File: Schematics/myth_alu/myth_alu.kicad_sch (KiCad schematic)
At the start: 5 parts, among them U1 74AHC273, U2 74AHC273, U3 SST39SF040, U4 74HC04, U5 SST39SF040

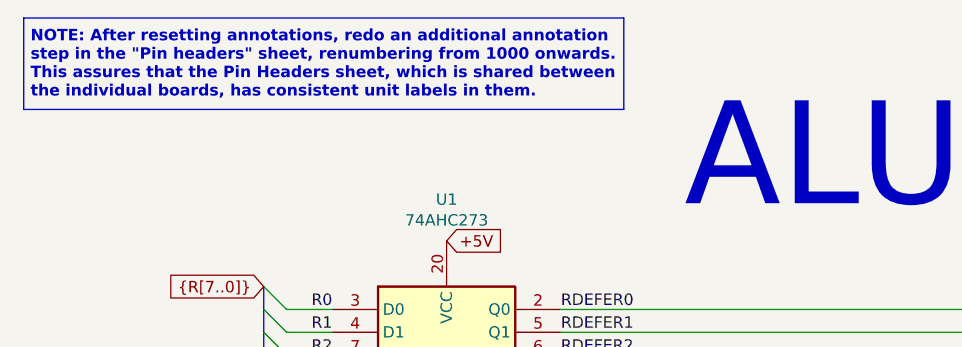
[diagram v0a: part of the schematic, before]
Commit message: Reduce number of shared headers
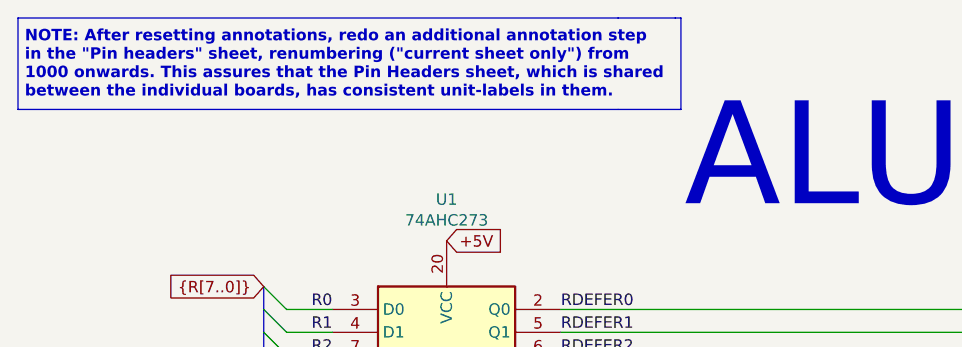
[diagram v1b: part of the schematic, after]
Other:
- note added: "NOTE: After resetting annotations, redo an additional annotation step in the "Pin headers" sheet, renumbering ("current sheet only") from 1000 onwards. This assures that the Pin Headers sheet, which is shared between the individual boards, has consistent unit-labels in them."
- note removed: "NOTE: After resetting annotations, redo an additional annotation step in the "Pin headers" sheet, renumbering from 1000 onwards. This assures that the Pin Headers sheet, which is shared between the individual boards, has consistent unit labels in them."

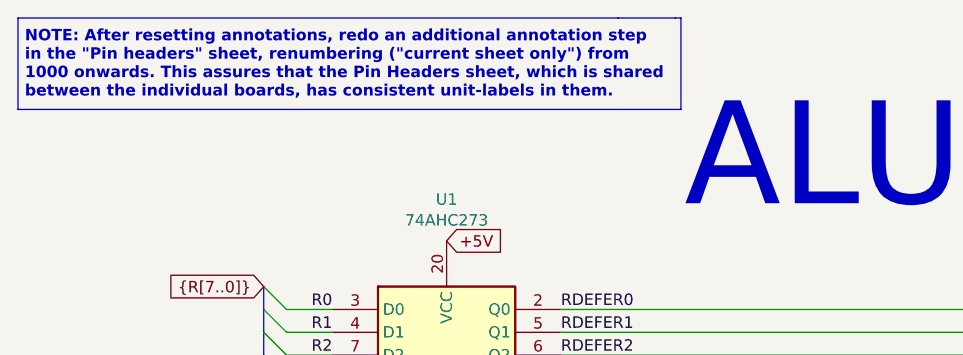
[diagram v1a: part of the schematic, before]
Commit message: Improve schematics for readability
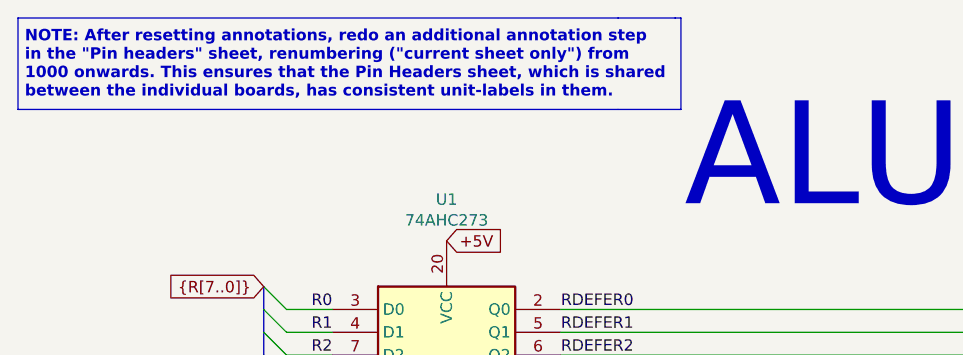
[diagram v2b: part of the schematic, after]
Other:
- note added: "NOTE: After resetting annotations, redo an additional annotation step in the "Pin headers" sheet, renumbering ("current sheet only") from 1000 onwards. This ensures that the Pin Headers sheet, which is shared between the individual boards, has consistent unit-labels in them."
- note removed: "NOTE: After resetting annotations, redo an additional annotation step in the "Pin headers" sheet, renumbering ("current sheet only") from 1000 onwards. This assures that the Pin Headers sheet, which is shared between the individual boards, has consistent unit-labels in them."
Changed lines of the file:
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@@
 		)
 	)
-	(text "NOTE: After resetting annotations, redo an additional annotation step\nin the \"Pin headers\" sheet, renumbering (\"current sheet only\") from\n1000 onwards. This assures that the Pin Headers sheet, which is shared\nbetween the individual boards, has consistent unit-labels in them."
+	(text "NOTE: After resetting annotations, redo an additional annotation step\nin the \"Pin headers\" sheet, renumbering (\"current sheet only\") from\n1000 onwards. This ensures that the Pin Headers sheet, which is shared\nbetween the individual boards, has consistent unit-labels in them."
 		(exclude_from_sim no)
 		(at 14.097 22.352 0)

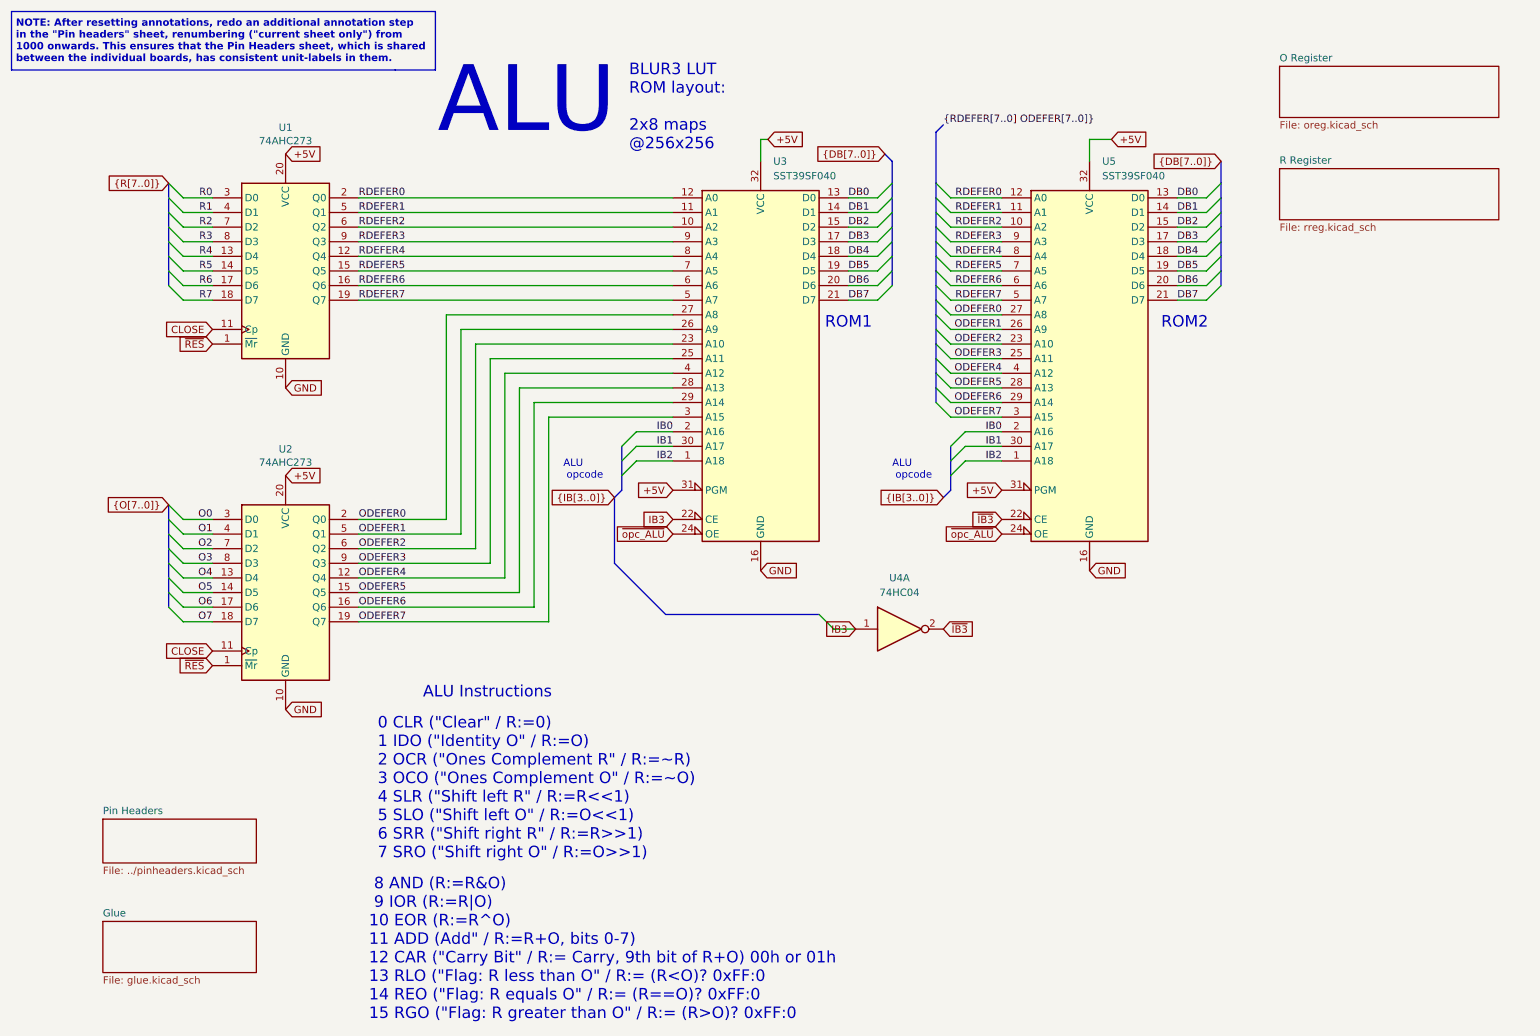
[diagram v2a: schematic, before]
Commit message: Change d to g
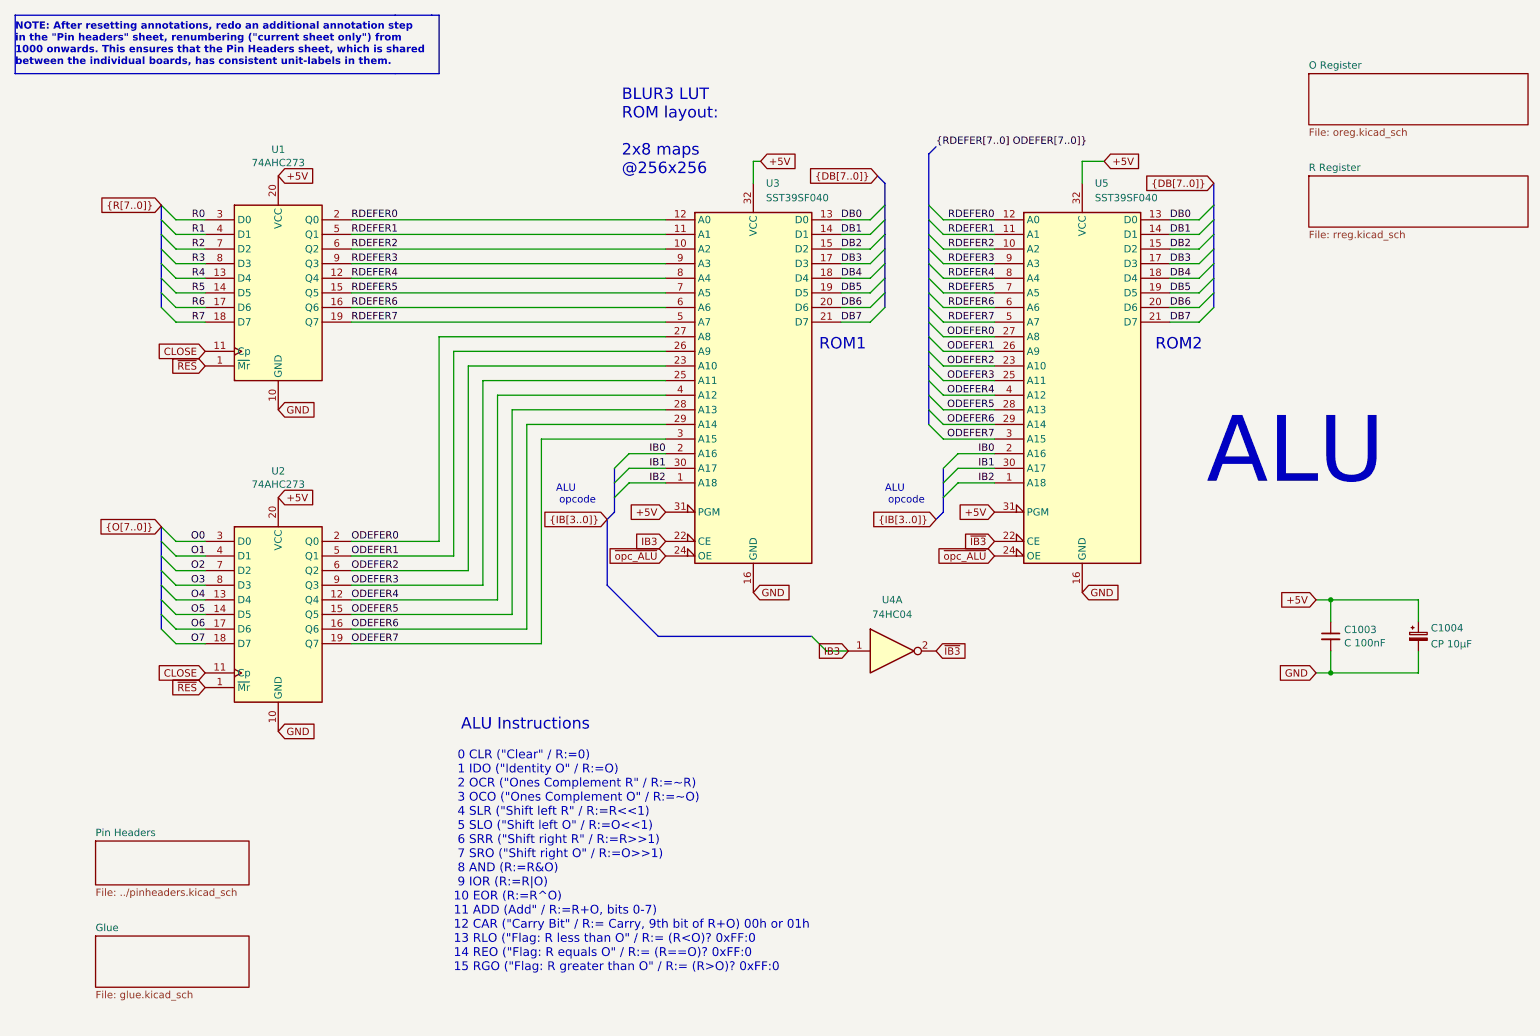
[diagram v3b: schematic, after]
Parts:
- added C1003: C 100nF, Capacitor_THT:C_Disc_D5.0mm_W2.5mm_P2.50mm, symbol Device:C_Small
- added C1004: CP 10μF, Capacitor_THT:CP_Radial_D6.3mm_P2.50mm, symbol Device:C_Polarized_Small
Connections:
- net +5V: now also C1003.1, C1004.1
- net GND: now also C1003.2, C1004.2
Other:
- note added: "0 CLR ("Clear" / R:=0) 1 IDO ("Identity O" / R:=O) 2 OCR ("Ones Complement R" / R:=~R) 3 OCO ("Ones Complement O" / R:=~O) 4 SLR ("Shift left R" / R:=R<<1) 5 SLO ("Shift left O" / R:=O<<1) 6 SRR ("Shift right R" / R:=R>>1) 7 SRO ("Shift right O" / R:=O>>1) 8 AND (R:=R&O) 9 IOR (R:=R|O) 10 EOR (R:=R^O) 11 ADD (Add" / R:=R+O, bits 0-7) 12 CAR ("Carry Bit" / R:= Carry, 9th bit of R+O) 00h or 01h 13 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"
- note removed: "0 CLR ("Clear" / R:=0) 1 IDO ("Identity O" / R:=O) 2 OCR ("Ones Complement R" / R:=~R) 3 OCO ("Ones Complement O" / R:=~O) 4 SLR ("Shift left R" / R:=R<<1) 5 SLO ("Shift left O" / R:=O<<1) 6 SRR ("Shift right R" / R:=R>>1) 7 SRO ("Shift right O" / R:=O>>1)"
- note removed: "8 AND (R:=R&O) 9 IOR (R:=R|O) 10 EOR (R:=R^O) 11 ADD (Add" / R:=R+O, bits 0-7) 12 CAR ("Carry Bit" / R:= Carry, 9th bit of R+O) 00h or 01h 13 RLO ("Flag: R less than O" / R:= (R<O)? 0xFF:0 14 REO ("Flag: R equals O" / R:= (R==O)? 0xFF:0 15 RGO ("Flag: R greater than O" / R:= (R>O)? 0xFF:0"
- moved on the sheet: U1, U2, U3, U4A, U5
